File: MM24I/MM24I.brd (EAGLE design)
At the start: 160 x 100 mm, 7 parts

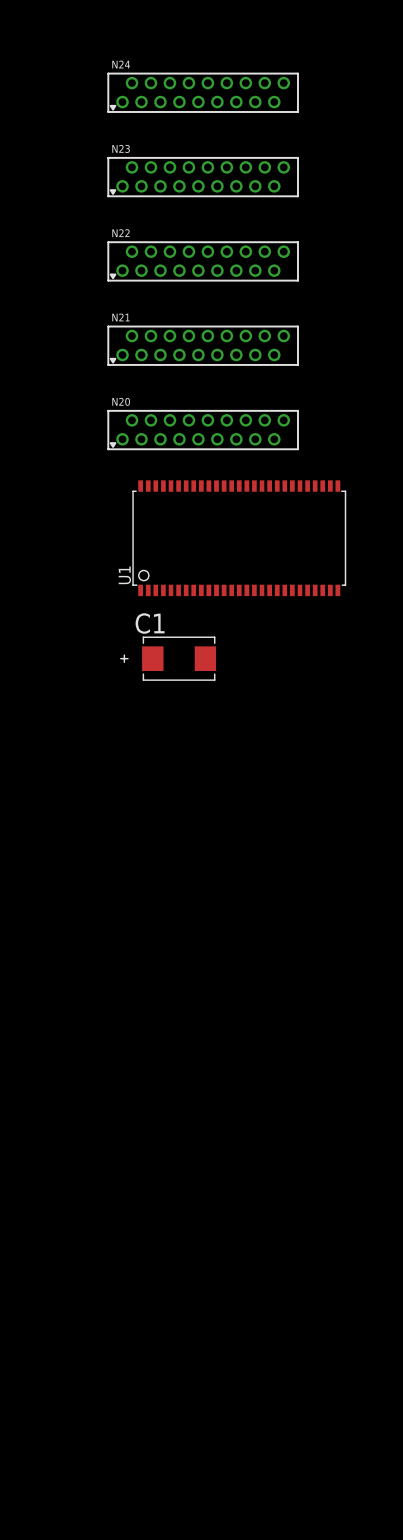
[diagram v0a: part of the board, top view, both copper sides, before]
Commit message: Add SN74LVC16T245 16-bit Bus Transceiver/Level Shifter
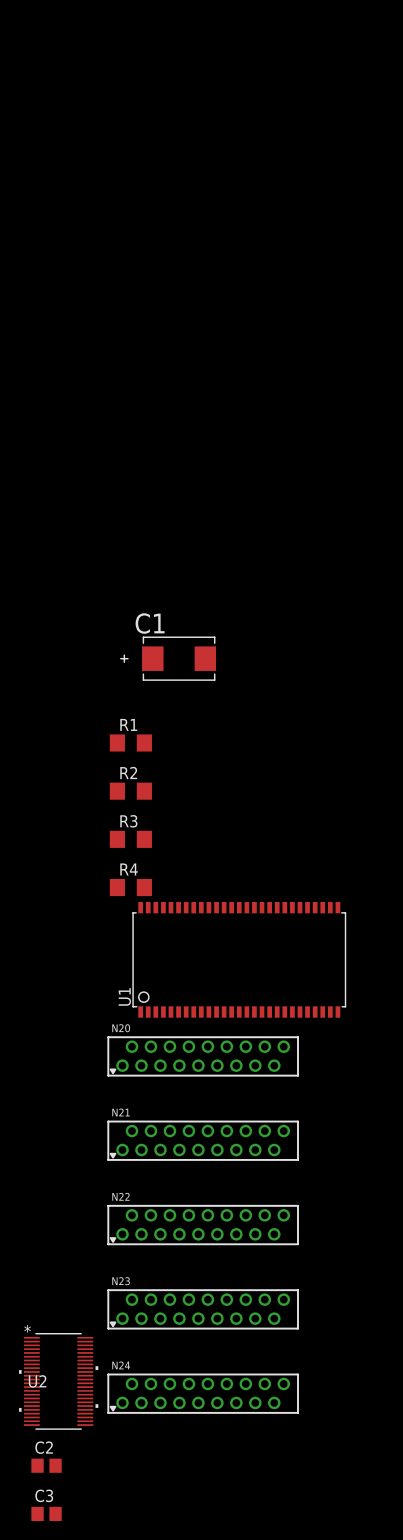
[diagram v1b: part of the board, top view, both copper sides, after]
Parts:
- added C2, C3: (no value), rcl:C0805
- added R1, R2, R3, R4: 10k, rcl:R1206
- added U2: SN74LVC16T245DGVR, MM24I:DGV48
- U1: value (none) -> CY14B104M; device Cypress Memory:TSOPII-54 -> MM24I:TSOPII-54
- moved N24 137.2 mm to (-22.9, -96.5)
- moved N23 119.4 mm to (-22.9, -87.6)
- moved N22 101.6 mm to (-22.9, -78.7)
- moved N21 83.8 mm to (-22.9, -69.8)
- moved N20 66.0 mm to (-22.9, -61.0)
- moved U1 44.4 mm to (-19.1, -50.8)
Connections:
- removed net MCS_MEM_06: N20.16, N21.16, N22.16, N23.16
- removed net MCS_MEM_08: N20.4, N21.4, N22.4, N24.4
- removed net MCS_MEM_09: N20.5, N21.5, N22.5, N23.5, N24.5
- removed net MCS_MEM_10: N20.7, N21.7, N22.7, N23.7, N24.7
- removed net MCS_MEM_11: N20.9, N21.9, N22.9, N23.9, N24.9
- removed net MCT_MEM_DONE: N20.15, N21.15, N22.15, N23.15, N24.15
- removed net MCT_STROBE: N20.13, N21.13, N22.13, N23.13, N24.13
- removed net MXB_MEM_TP3: N20.18, N21.18, N22.18, N23.18, N24.18
- removed net MXB_START_MEMORY: N20.11, N21.11, N22.11, N23.11, N24.11
- new net !WE: U1.19, U2.1, U2.24
- new net +5V: C3.2
- new net MCS-MEM-00-H: N23.5
- new net MCS-MEM-01-H: N23.7
- new net MCS-MEM-02-H: N23.9
- new net MCS-MEM-03-H: N23.11
- new net MCS-MEM-04-H: N23.13
- new net MCS-MEM-05-H: N23.15
- new net MCS-MEM-06-H: N23.16
- new net MCS-MEM-07-H: N23.18
- new net MCS-MEM-08-H: N24.4
- new net MCS-MEM-09-H: N24.5
- new net MCS-MEM-10-H: N24.7
- new net MCS-MEM-11-H: N24.9
- new net MCT-MEM-DONE-L: N24.15
- new net MCT-STROBE-L: N24.13
- new net MXB-BMA-00-H: N20.9
- new net MXB-BMA-01-H: N20.11
- new net MXB-BMA-02-H: N20.13
- new net MXB-BMA-03-H: N20.15
- new net MXB-BMA-04-H: N20.16
- new net MXB-BMA-05-H: N20.18
- new net MXB-BMA-06-H: N21.4
- new net MXB-BMA-07-H: N21.5
- new net MXB-BMA-08-H: N21.7
- new net MXB-BMA-09-H: N21.9
- new net MXB-BMA-10-H: N21.11
- new net MXB-BMA-11-H: N21.13
- new net MXB-MCBMB-00-H: N21.15
- new net MXB-MCBMB-01-H: N21.16
- new net MXB-MCBMB-02-H: N21.18
- new net MXB-MCBMB-03-H: N20.4
- new net MXB-MCBMB-04-H: N20.5
- new net MXB-MCBMB-05-H: N20.7
- new net MXB-MCBMB-06-H: N22.9
- new net MXB-MCBMB-07-H: N22.11
- new net MXB-MCBMB-08-H: N22.13
- new net MXB-MCBMB-09-H: N22.15
- new net MXB-MCBMB-10-H: N22.16
- new net MXB-MCBMB-11-H: N22.18
- new net MXB-MEM-TP3-H: N24.18
- new net MXB-START-MEMORY-H: N24.11
- new net MXF-EA-00-H: N22.4
- new net MXF-EA-01-H: N22.5
- new net MXF-EA-02-H: N22.7
- new net N$10: R4.1, U1.46
- new net N$11: U1.17, U2.38
- new net N$12: R1.1, U1.43
- new net N$13: U1.18, U2.37
- new net N$14: U1.37, U2.36
- new net N$15: U1.38, U2.35
- new net N$16: U1.39, U2.33
- new net N$17: U1.40, U2.32
- new net N$18: U2.2
- new net N$19: U2.3
- new net N$20: U2.5
- new net N$21: U2.6
- new net N$22: U2.8
- new net N$23: U2.9
- new net N$24: U2.11
- new net N$25: U2.12
- new net N$26: U2.13
- new net N$27: U2.14
- new net N$28: U2.16
- new net N$29: U2.17
- new net N$3: U1.10, U2.46
- new net N$30: C3.1, U2.18, U2.7
- new net N$31: C2.1, U2.31, U2.42
- new net N$4: U1.11, U2.44
- new net N$5: U1.12, U2.43
- new net N$6: U1.15, U2.41
- new net N$7: U1.16, U2.40
- new net N$8: R2.1, U1.44
- new net N$9: R3.1, U1.45
- net GND: now also R1.2, R2.2, R3.2, R4.2, U2.10, U2.15, U2.19, U2.20, U2.21, U2.22, U2.23, U2.25, U2.26, U2.27, U2.28, U2.29, U2.30, U2.34, U2.39, U2.4, U2.45, U2.48
- net N$2: now also U1.9, U2.47; no longer U1.34, U1.35, U1.50, U1.51, U1.52
- net VCC: now also C2.2
